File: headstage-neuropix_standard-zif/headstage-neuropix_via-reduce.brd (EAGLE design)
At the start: 21.2 x 49.8 mm, 147 parts, among them J1 302-S101, J2 X.FL-R-SMT-1(02), J3 FH23-45S-0.3SHW(05), J5 77311-118-02LF, J6 FH23-45S-0.3SHW(05), U1 10M08SAM15317G, U10 PL133-27GC-R, U11 TS4231, U12 TS4231, U13 TS4231, U2 ASCO2-24.000MHZ-EK-T3, U3 MAX4945AELA+T, U4 DS90UB933_WQFN, U5 NCP161BMX330, U6 TPS8268180, U7 TLV70712, U8 BNO055, U9 DSC6102MI2A-093.6000, X2 OE-LOGO_14X10

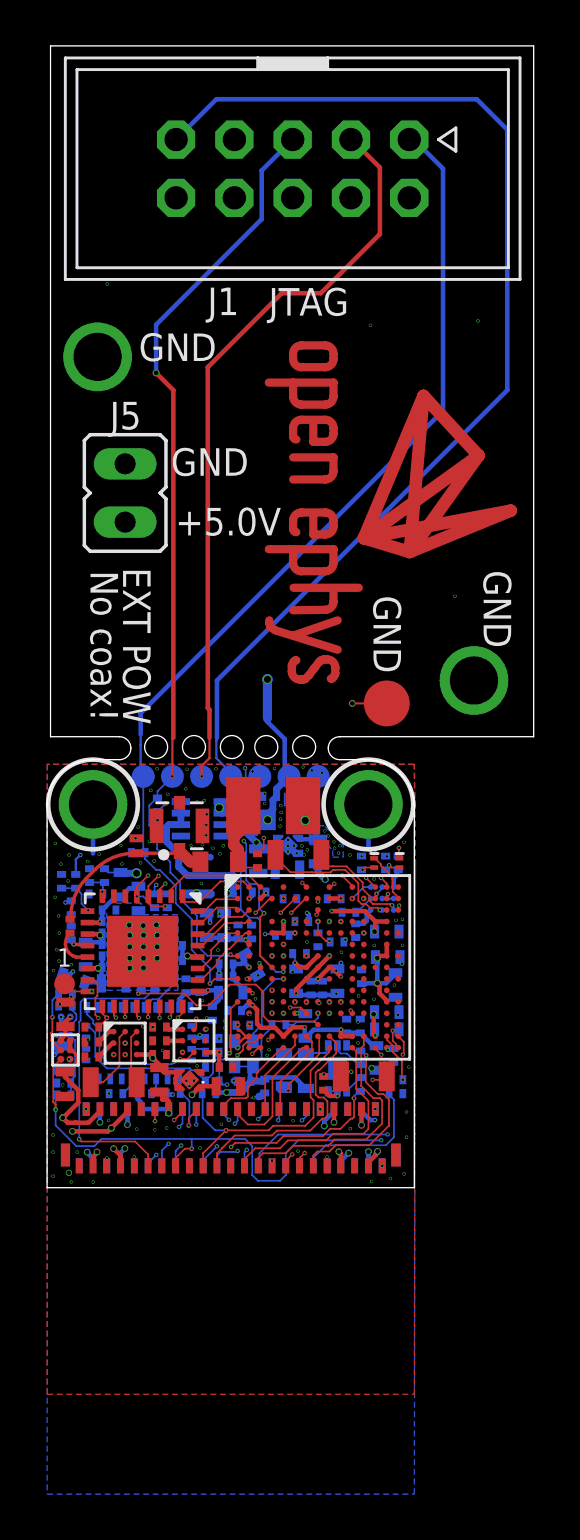
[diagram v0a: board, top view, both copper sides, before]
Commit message: Moved X.FL coax connector up 0.5 mm following OEPS feedback
- Allows more tolerance for passives under it
- Did this for both headstage variants
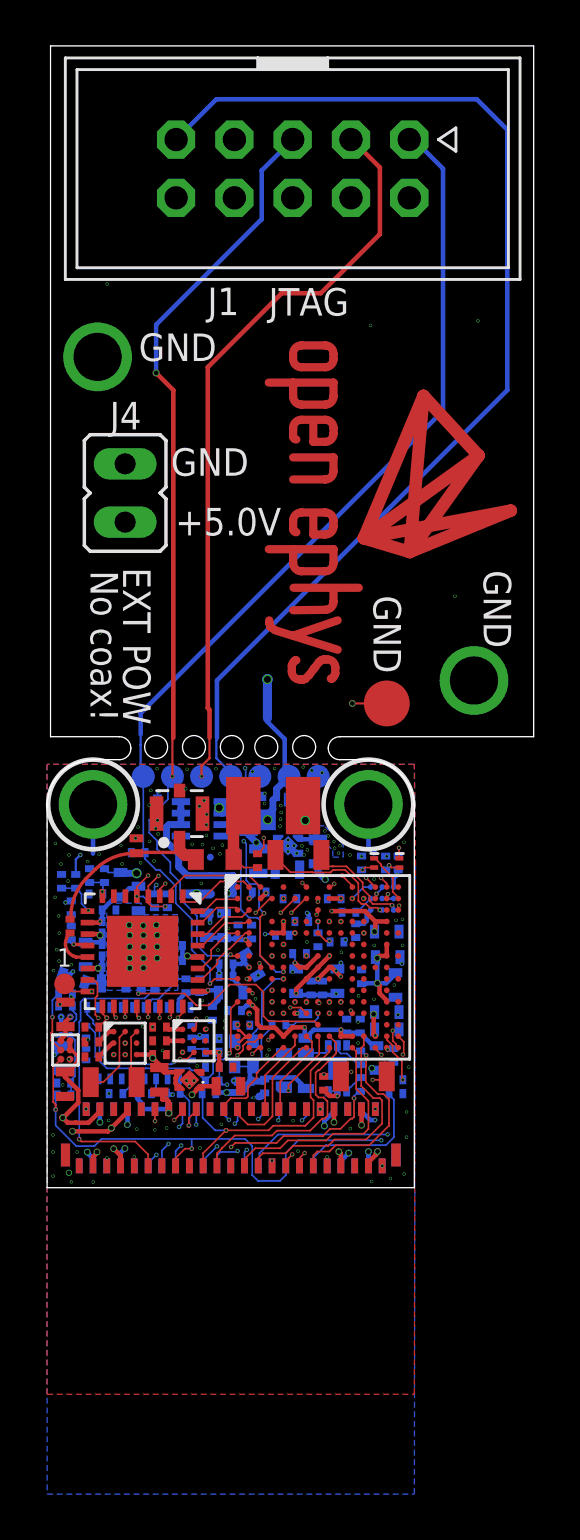
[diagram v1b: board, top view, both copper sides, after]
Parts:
- removed C66: 10uF, jonnew:0402TW
- removed C67: 1uF, jonnew:0201T
- removed J6: FH23-45S-0.3SHW(05), jonnew:1-2013496-8
- added C56: 10nF, jonnew:0201T
- added C60: 1uF, jonnew:0201T
- added J4: 77311-118-02LF, jonnew:JP2
- C24, C26, C28: value 0.1uF -> 10uF; device jonnew:0201T -> jonnew:0402TW
- C25: value 10uF -> 1uF; device jonnew:0402TW -> jonnew:0201T
- C27, C32, C64, C65: value 10uF -> 0.1uF; device jonnew:0402TW -> jonnew:0201T
- C30: value 10nF -> 1nF
- C31, C49: value 10nF -> 0.1uF
- C34, C40, C59: value 0.1uF -> 10nF
- C36, C37: value 10nF -> 10uF; device jonnew:0201T -> jonnew:0402TW
- C38: value 0.1uF -> 1uF
- C41, C42: value 10uF -> 10nF; device jonnew:0402TW -> jonnew:0201T
- C43: value 0.1uF -> 1nF
- C44: value 47nF -> 0.1uF
- C45: value 4.7uF -> 0.1uF; device jonnew:0402T -> jonnew:0201T
- C46: value 10uF -> 0.1uF; device jonnew:0402T -> jonnew:0201T
- C48, C54: value 1uF -> 10uF; device jonnew:0201T -> jonnew:0402TW
- C50: value 0.1uF -> 47nF
- C51: device jonnew:0402T -> jonnew:0402TW
- C52: value 10nF -> 4.7uF; device jonnew:0201T -> jonnew:0402T
- C53: value 1uF -> 10uF; device jonnew:0201T -> jonnew:0402T
- C58: value 0.1uF -> 10uF; device jonnew:0201T -> jonnew:0402T
- C62: value 1nF -> 1uF
- C63: value 1nF -> 0.1uF
- J3: value FH23-45S-0.3SHW(05) -> 1-2013496-8
- J5: value 77311-118-02LF -> 1-2013496-8; device jonnew:JP2 -> jonnew:1-2013496-8
- R21: value 49.9 -> 6.6k
- R23: value 10k -> 49.9
- R24: value 100k -> 10k
- R25: value 2k -> 10k
- R26: value 22 -> 100k
- R27: value 22 -> 2k
- R28: value 20k -> 22
- R29: value 100 -> 20k
- R30: value 15k -> 100
- R31: value 15k -> 22
- R33: value 20k -> 15k
- R34: value 100 -> 15k
- R35: value 6.6k -> 20k
- R36: value 10k -> 100
- U10: value PL133-27GC-R -> BNO055; device jonnew:DFN6_2X1.3_PAD -> jonnew:LGA-28-3.8X5.2
- U11: value TS4231 -> DSC6102MI2A-093.6000; device jonnew:WLCSP3X3 -> jonnew:VFLGA4-2.0X1.6
- U12: value TS4231 -> PL133-27GC-R; device jonnew:WLCSP3X3 -> jonnew:DFN6_2X1.3_PAD
- U14, U15: value (none) -> TS4231; device jonnew:WLCSP6-1X1.2 -> jonnew:WLCSP3X3
- U4: value DS90UB933_WQFN -> ADP7112ACBZ-1.8-R7; device jonnew:WQFN32-5X5 -> jonnew:WLCSP6-1X1.2
- U5: value NCP161BMX330 -> DS90UB933_WQFN; device jonnew:X2SON -> jonnew:WQFN32-5X5
- U6: value TPS8268180 -> NCP161BMX330; device jonnew:MICROSIP9-3X2.3 -> jonnew:X2SON
- U7: value TLV70712 -> TPS8268180; device jonnew:X2SON -> jonnew:MICROSIP9-3X2.3
- U8: value BNO055 -> TLV70712; device jonnew:LGA-28-3.8X5.2 -> jonnew:X2SON
- U9: value DSC6102MI2A-093.6000 -> ADP7112ACBZ-1.2-R7; device jonnew:VFLGA4-2.0X1.6 -> jonnew:WLCSP6-1X1.2
- moved J5 28.4 mm to (0.00, 1.65), flipped to the bottom, turned to 0 degrees
- moved C65 15.9 mm to (7.30, 14.8), flipped to the bottom
- moved C51 15.3 mm to (-7.30, 6.34), turned to 270 degrees
- moved R26 14.9 mm to (-6.15, 14.3), turned to 90 degrees
- moved U15 14.9 mm to (6.60, 13.3), turned to 180 degrees
- moved R35 14.5 mm to (7.20, 5.40)
- moved R36 13.6 mm to (7.20, 4.80), flipped to the bottom
- moved C55 13.0 mm to (-7.37, 14.1), turned to 90 degrees
- moved C62 12.9 mm to (5.45, 11.9), turned to 270 degrees
- moved R32 12.9 mm to (-6.05, 6.40), flipped to the top, turned to 0 degrees
- moved U13 12.9 mm to (-4.60, 7.00), flipped to the top, turned to 0 degrees
- moved C58 12.1 mm to (3.05, 17.6), flipped to the bottom
- moved C48 11.5 mm to (-0.10, 5.12), flipped to the top, turned to 0 degrees
- moved C52 11.4 mm to (-4.02, 13.3), flipped to the bottom
- moved C61 11.1 mm to (-3.10, 7.70), flipped to the top, turned to 180 degrees
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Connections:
- removed net N$9 (its old number): R30.2, U11.B1
- new net N$29: R34.2, U15.B1
- net !IMU_BL: now also R24.2, U10.4; no longer R22.2, U8.4
- net !IMU_RESET: now also R20.1, U10.11; no longer R19.1, U8.11
- net +1V2: now also C48.1, J5.38, J5.39, U8.1; no longer C42.1, J6.38, J6.39, U7.1
- net +1V8: now also C31.1, C34.1, C41.1, C45.1, C53.1, C56.2, C59.2, J5.42, J5.43, R25.1, U11.4, U12.5, U12.6, U5.11, U5.28, U7.A1, U7.A2; no longer C28.1, C30.1, C36.1, C39.1, C46.1, C49.2, C52.2, J6.42, J6.43, R23.1, U10.5, U10.6, U4.11, U4.28, U6.A1, U6.A2, U9.4
- net +3V3: now also C27.1, C32.1, C35.1, C37.1, C47.1, C63.1, C64.1, R20.2, R24.1, U10.28, U10.3, U14.C3, U15.C3, U4.A1, U5.25, U6.1, U8.4, U9.A1; no longer C26.1, C31.1, C33.1, C41.1, C57.1, C58.1, C59.1, R19.2, R20.1, U11.C3, U12.C3, U14.A1, U15.A1, U4.25, U5.1, U7.3, U7.4, U8.28
- net 1V2A: now also C51.1, J5.7, J5.8, U9.A2, U9.B2; no longer C66.1, J6.7, J6.8, U15.A2, U15.B2
- net 1V8A: now also C33.1, J5.3, J5.4, U4.A2, U4.B2; no longer C64.1, J6.3, J6.4, U14.A2, U14.B2
- net BNO_SCL: now also U10.19; no longer U8.19
- net BNO_SDA: now also U10.20; no longer U8.20
- net CAL_A_1KHZ: now also R29.1; no longer R28.1
- net CAL_B_1KHZ: now also R35.1; no longer R33.1
- net CAL_SIGNAL_A: now also R29.2, R30.1; no longer R28.2, R29.1
- net CAL_SIGNAL_A1: now also J5.11, R35.2, R36.1; no longer J6.11, R33.2, R34.1
- net GND: now also C34.2, C39.1, C43.2, C44.2, C52.2, C56.1, C59.1, C60.2, J4.2, J5.1, J5.10, J5.13, J5.14, J5.17, J5.20, J5.23, J5.26, J5.29, J5.32, J5.34, J5.36, J5.37, J5.41, J5.44, J5.45, J5.5, J5.6, J5.9, R19.2, R23.1, R26.2, R30.2, R33.1, R34.1, U10.15, U10.16, U10.17, U10.18, U10.2, U10.25, U10.5, U10.6, U11.2, U12.3, U14.B2, U14.B3, U15.B2, U15.B3, U4.C2, U5.6, U5.7, U6.2, U6.PAD, U7.C1, U7.C2, U7.C3, U8.PAD, U9.C2; no longer C34.1, C39.2, C49.1, C50.2, C52.1, C59.2, C66.2, C67.2, J6.1, J6.10, J6.13, J6.14, J6.17, J6.2, J6.20, J6.23, J6.26, J6.29, J6.32, J6.34, J6.36, J6.37, J6.41, J6.44, J6.45, J6.5, J6.6, J6.9, R21.1, R24.2, R29.2, R30.1, R31.1, R34.2, U10.3, U11.B2, U11.B3, U12.B2, U12.B3, U14.C2, U15.C2, U4.6, U4.7, U4.PAD, U5.2, U6.C1, U6.C2, U6.C3, U7.2, U7.PAD, U8.15, U8.16, U8.17, U8.18, U8.25, U8.5, U8.6, U9.2
- net I2C_SCL_B: now also J5.19; no longer J6.19
- net I2C_SDA_B: now also J5.18; no longer J6.18
- net LH_DATA0: now also U14.C1; no longer U12.C1
- net LH_DATA1: now also U13.C1; no longer U11.C1
- net LH_DATA2: now also U15.C1; no longer U13.C1
- net LH_ENV0: now also U14.C2; no longer U12.C2
- net LH_ENV1: now also U13.C2; no longer U11.C2
- net LH_ENV2: now also U15.C2; no longer U13.C2
- net MIDFILT: now also R27.1; no longer R25.1
- net N$1: now also U11.3, U12.1; no longer U10.1, U9.3
- net N$12: now also C60.1, U13.A1; no longer C53.1, U11.A1
- net N$13: now also C58.1, R27.2; no longer C51.1, R25.2
- net N$14: now also U14.A3; no longer U12.A3
- net N$15: now also U14.A2; no longer U12.A2
- net N$16: now also R33.2, U14.B1; no longer R31.2, U12.B1
- net N$2: now also R28.1, U12.4; no longer R26.1, U10.4
- net N$26: now also U15.A3; no longer U13.A3
- net N$27: now also U15.A2; no longer U13.A2
- net N$28: now also C49.2, U5.13; no longer C43.2, U4.13
- net N$3: now also R31.2; no longer R27.2
- net N$30: now also C55.1, R22.2, U5.9; no longer C48.1, R20.2, U4.9
- net N$31: now also C50.2, U5.12; no longer C44.2, U4.12
- net N$32: now also C50.1, R23.2; no longer C44.1, R21.2
- net N$33: now also C57.1, R25.2, R26.1, U5.8; no longer C50.1, R23.2, R24.1, U4.8
- net N$34: now also C40.1, C44.1, C52.1, U5.10; no longer C35.1, C38.1, C45.1, U4.10
- net N$35: now also C42.1, C46.1, C54.1, U5.14; no longer C37.1, C40.1, C47.1, U4.14
- net N$36: now also C61.1, U14.A1; no longer C54.1, U12.A1
- net N$37: now also C62.1, U15.A1; no longer C55.1, U13.A1
- net N$38: now also C26.1, C28.1, C36.1, U6.3, U6.4, U7.A3, U7.B1, U7.B2, U7.B3; no longer C25.1, C27.1, C32.1, U5.3, U5.4, U6.A3, U6.B1, U6.B2, U6.B3
- net N$39: now also C30.1, U4.B1; no longer C62.1, U14.B1
- net N$40: now also C43.1, U9.B1; no longer C63.1, U15.B1
- net N$41: now also C38.1, R21.1, U9.C1; no longer C67.1, R35.1, U15.C1
- net N$5: now also J5.35, R28.2; no longer J6.35, R26.2
- net N$6: now also R31.1, U12.2; no longer R27.1, U10.2
- net N$67: now also C39.2, U10.9; no longer C34.2, U8.9
- net N$7: now also U13.A3; no longer U11.A3
- net N$8: now also U13.A2; no longer U11.A2
- net NP_OSC_EN: now also U11.1; no longer U9.1
- net NRST: now also J5.15, R21.2, U4.C1; no longer J6.15, R35.2, U14.C1
- net OSC_PDOWN_N_B: now also J5.12; no longer J6.12
- net PSB_CLK_B: now also J5.33; no longer J6.33
- net PSB_DATA_0_B: now also J5.31; no longer J6.31
- net PSB_DATA_1_B: now also J5.30; no longer J6.30
- net PSB_DATA_2_B: now also J5.28; no longer J6.28
- net PSB_DATA_3_B: now also J5.27; no longer J6.27
- net PSB_DATA_4_B: now also J5.25; no longer J6.25
- net PSB_DATA_5_B: now also J5.24; no longer J6.24
- net PSB_DATA_6_B: now also J5.22; no longer J6.22
- net PSB_SYNC_B: now also J5.21; no longer J6.21
- net REC_NRST_B: now also J5.16; no longer J6.16
- net SER_DIN0: now also U5.19; no longer U4.19
- net SER_DIN1: now also U5.20; no longer U4.20
- net SER_DIN10: now also U5.31; no longer U4.31
- net SER_DIN11: now also U5.32; no longer U4.32
- net SER_DIN2: now also U5.21; no longer U4.21
- net SER_DIN3: now also U5.22; no longer U4.22
- net SER_DIN4: now also U5.23; no longer U4.23
- net SER_DIN5: now also U5.24; no longer U4.24
- net SER_DIN6: now also U5.26; no longer U4.26
- net SER_DIN7: now also U5.27; no longer U4.27
- net SER_DIN8: now also U5.29; no longer U4.29
- net SER_DIN9: now also U5.30; no longer U4.30
- net SER_GPIO0: now also U5.15; no longer U4.15
- net SER_GPIO1: now also U5.16; no longer U4.16
- net SER_GPIO2: now also R19.1, U5.17; no longer R36.1, U4.17
- net SER_GPIO3: now also U5.18; no longer U4.18
- net SER_HSYNC: now also U5.1; no longer U4.1
- net SER_PCLK: now also U5.3; no longer U4.3
- net SER_SCL: now also U5.4; no longer U4.4
- net SER_SDA: now also U5.5; no longer U4.5
- net SER_VSYNC: now also U5.2; no longer U4.2
- net SIGOUT: now also C49.1; no longer C43.1
- net VCOAX: now also C25.1, J4.1; no longer C61.1, J5.1
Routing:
- net N$29: track 0.00 -> 0.90 mm
- net N$9 (its old number): track 0.90 -> 0.00 mm
- net GND: vias 171 -> 173
